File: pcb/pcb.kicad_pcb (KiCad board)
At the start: 2 copper layers, 7 parts, among them J1 Conn_01x02, J2 Conn_01x04_Male, U1 MCP73811T-420I-OT, U2 LD39050PU33R

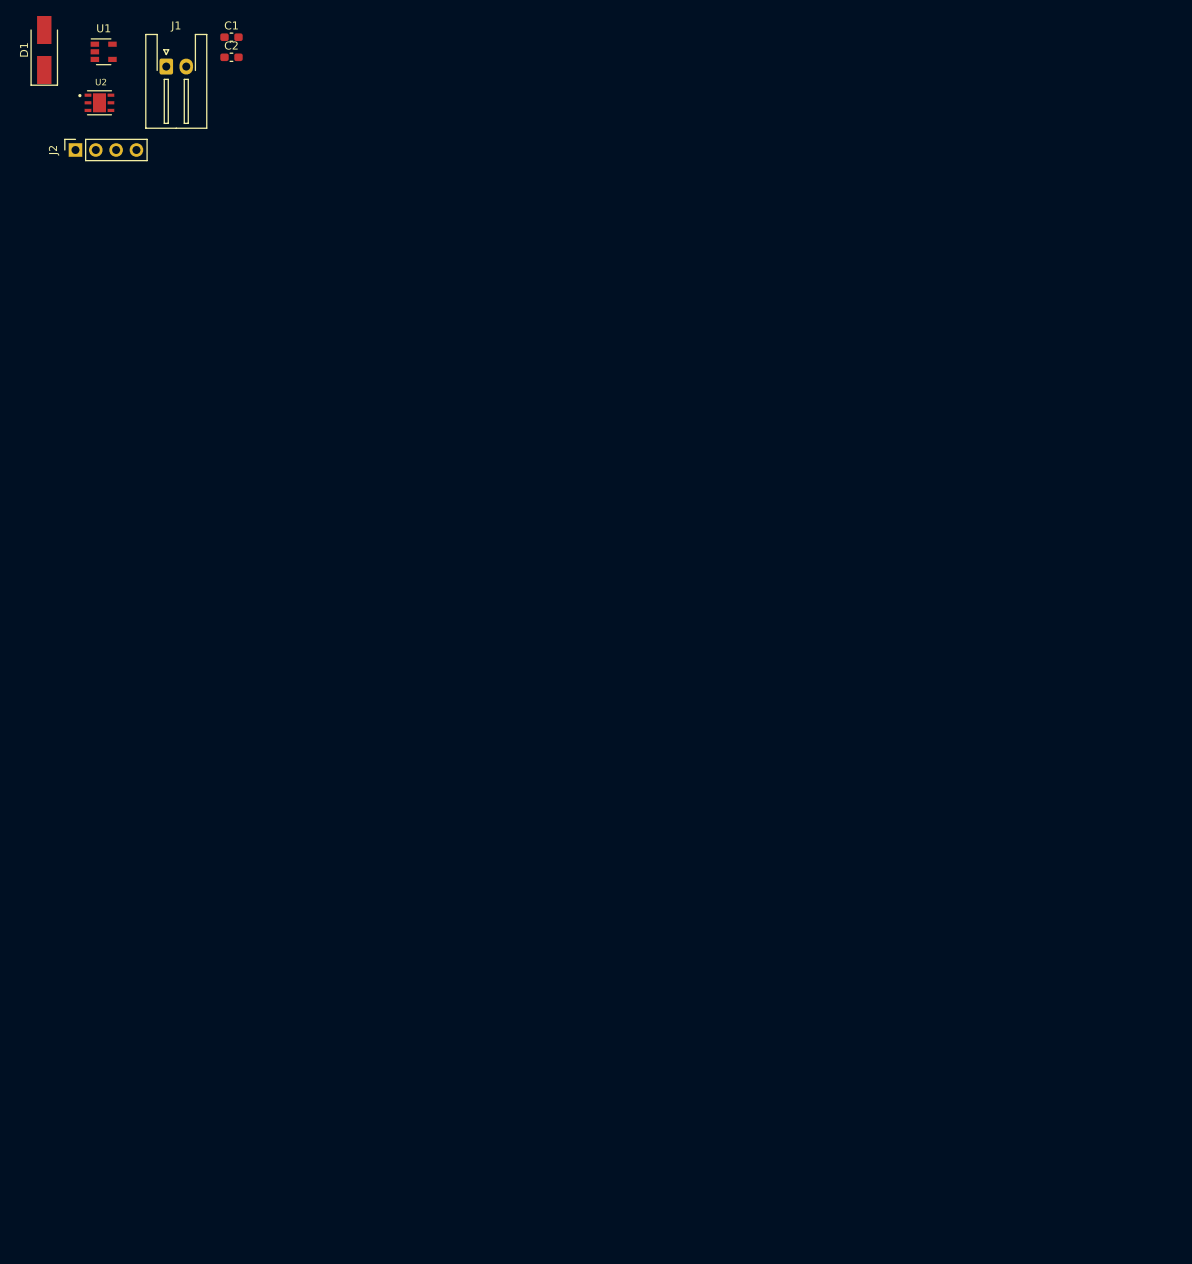
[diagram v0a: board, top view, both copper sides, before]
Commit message: finish the shcematic design
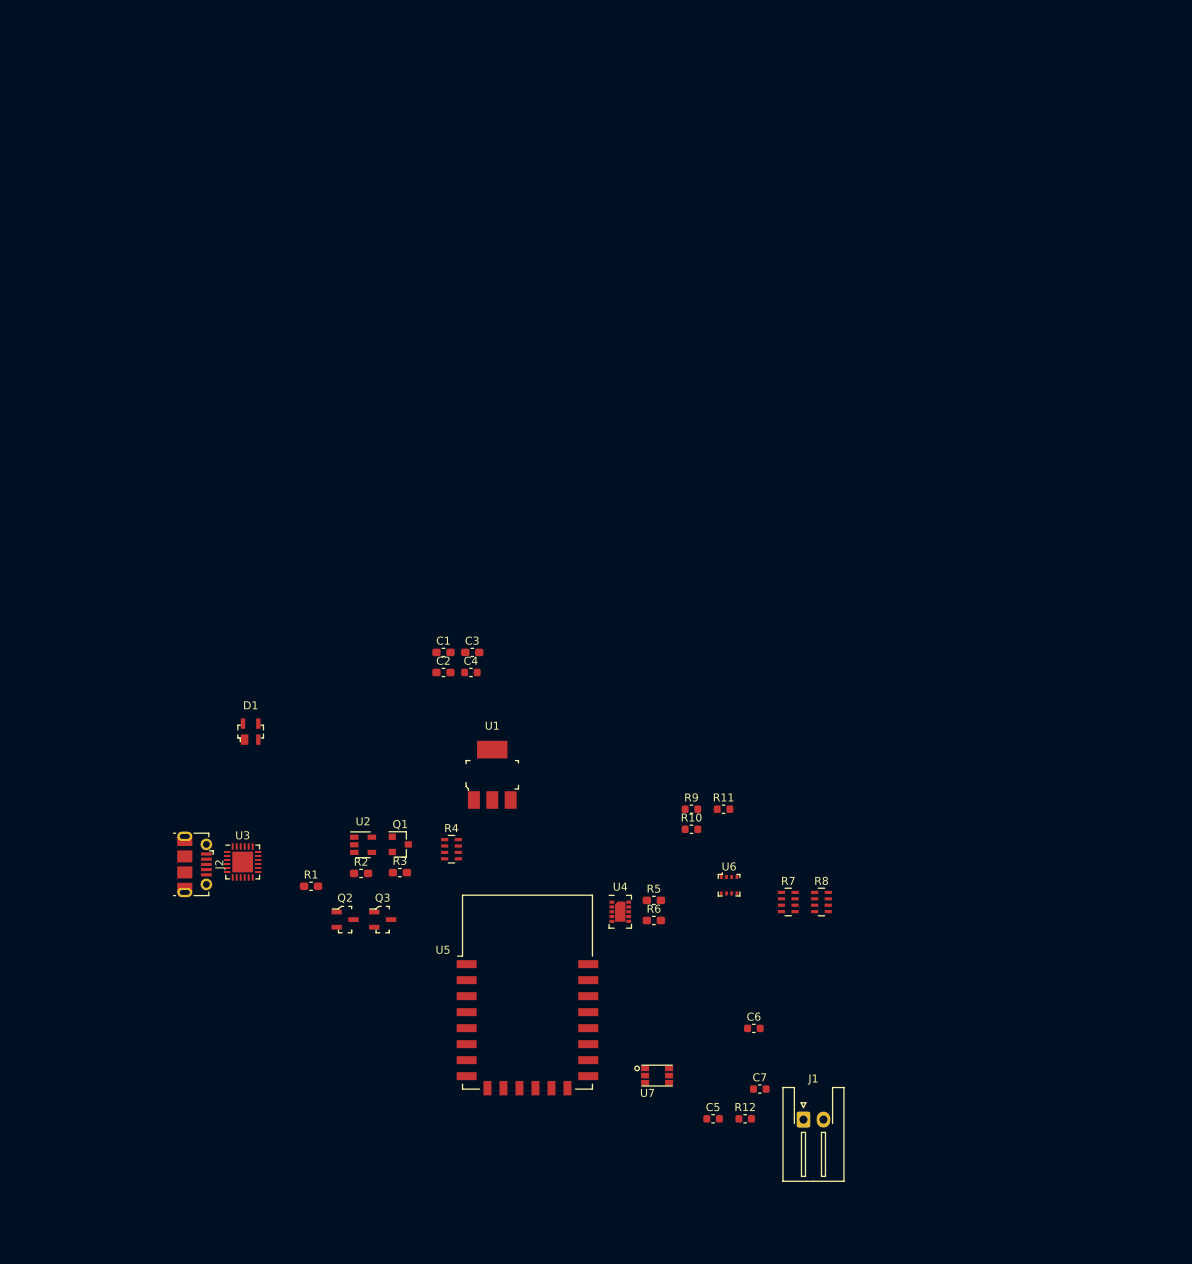
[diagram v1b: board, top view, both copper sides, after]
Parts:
- added C3: 10u, Capacitor_SMD:C_0603_1608Metric_Pad1.05x0.95mm_HandSolder, F.Cu at (53.2, 21.4)
- added C4: 100nF, Capacitor_SMD:C_0603_1608Metric, F.Cu at (53.0, 23.9)
- added C5: 100n, Capacitor_SMD:C_0603_1608Metric, F.Cu at (83.3, 79.7)
- added C6: 100n, Capacitor_SMD:C_0603_1608Metric, F.Cu at (88.4, 68.4)
- added C7: 100n, Capacitor_SMD:C_0603_1608Metric, F.Cu at (89.1, 76.0)
- added Q1: Si2371EDS, Package_TO_SOT_SMD:SOT-23, F.Cu at (44.2, 45.4)
- added Q2: MMBT2222A-TP, digikey-footprints:SOT-23-3, F.Cu at (37.3, 54.8)
- added Q3: MMBT2222A-TP, digikey-footprints:SOT-23-3, F.Cu at (42.0, 54.8)
- added R1: 2k, Resistor_SMD:R_0603_1608Metric_Pad1.05x0.95mm_HandSolder, F.Cu at (33.0, 50.6)
- added R10: 10k, Resistor_SMD:R_0603_1608Metric, F.Cu at (80.6, 43.5)
- added R11: 10k, Resistor_SMD:R_0603_1608Metric, F.Cu at (84.6, 41.0)
- added R12: 10k, Resistor_SMD:R_0603_1608Metric, F.Cu at (87.3, 79.7)
- added R2: 10k, Resistor_SMD:R_0603_1608Metric_Pad1.05x0.95mm_HandSolder, F.Cu at (39.3, 49.0)
- added R3: 10k, Resistor_SMD:R_0603_1608Metric_Pad1.05x0.95mm_HandSolder, F.Cu at (44.1, 48.9)
- added R4: R_Pack04_Split, Resistor_SMD:R_Array_Concave_4x0603, F.Cu at (50.6, 46.0)
- added R5: 100k, Resistor_SMD:R_0603_1608Metric_Pad1.05x0.95mm_HandSolder, F.Cu at (75.9, 52.4)
- added R6: 100k, Resistor_SMD:R_0603_1608Metric_Pad1.05x0.95mm_HandSolder, F.Cu at (75.9, 54.9)
- added R7: 10k, Resistor_SMD:R_Array_Concave_4x0603, F.Cu at (92.7, 52.6)
- added R8: 10k, Resistor_SMD:R_Array_Concave_4x0603, F.Cu at (96.8, 52.6)
- added R9: 10k, Resistor_SMD:R_0603_1608Metric, F.Cu at (80.6, 41.0)
- added U3: CP2104, Package_DFN_QFN:QFN-24-1EP_4x4mm_P0.5mm_EP2.6x2.6mm, F.Cu at (24.5, 47.6)
- added U4: CCS811, Package_LGA:AMS_LGA-10-1EP_2.7x4mm_P0.6mm, F.Cu at (71.7, 53.8)
- added U5: ESP-12F, RF_Module:ESP-12E, F.Cu at (60.1, 63.9)
- added U6: BME280, digikey-footprints:Pressure_Sensor_LGA-8_2.5x2.5mm_BME280, F.Cu at (85.3, 50.5)
- added U7: TSL2561, Kevin_Lutzer:TSL2561, F.Cu at (76.3, 74.3)
- C1: value 1uf -> 1u
- C2: value 1uf -> 10u
- D1: value D_Schottky -> SP0503BAHTG; footprint Diode_SMD:D_SMA_Handsoldering -> digikey-footprints:SOT-143-4
- J2: value Conn_01x04_Male -> USB_B_Micro; footprint Connector_PinSocket_2.54mm:PinSocket_1x04_P2.54mm_Vertical -> Connector_USB:USB_Micro-B_Molex-105017-0001
- U1: value MCP73811T-420I-OT -> LD1117S33CTR; footprint Package_TO_SOT_SMD:SOT-23-5 -> digikey-footprints:SOT-223
- U2: value LD39050PU33R -> MCP73831-2-OT; footprint LD39050PU33R:SON95P300X300X100-7N -> Package_TO_SOT_SMD:SOT-23-5
- moved J1 153.9 mm to (94.6, 79.8)
- moved U1 102.6 mm to (55.7, 36.7)
- moved U2 98.4 mm to (39.5, 45.5)
- moved J2 90.5 mm to (18.5, 47.9), turned to 270 degrees
- moved D1 89.0 mm to (25.5, 31.3), turned to 0 degrees
- moved C1 81.3 mm to (49.6, 21.4)
- moved C2 81.3 mm to (49.6, 23.9)
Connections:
- D1 pad 1: +5V -> GND
- D1 pad 2: +BATT -> Net-(D1-Pad2)
- J2 pad 1: (no net) -> +5V
- J2 pad 2: (no net) -> Net-(J2-Pad2)
- J2 pad 3: (no net) -> Net-(D1-Pad2)
- J2 pad 4: GND -> (no net)
- U1 pad 1: +5V -> GND
- U1 pad 2: GND -> +3V3
- U1 pad 3: +BATT -> +5V
- U1 pad 4: +5V -> +3V3
- U2 pad 1: +5V -> nBAT_STAT
- U2 pad 3: (no net) -> +BATT
- U2 pad 4: +3V3 -> +5V
- U2 pad 5: (no net) -> Net-(R1-Pad1)

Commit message: get the update done on the pcb design, finish it
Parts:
- removed R10, R11, R12: 10k, Resistor_SMD:R_0603_1608Metric
- removed R3: 10k, Resistor_SMD:R_0603_1608Metric_Pad1.05x0.95mm_HandSolder
- added D2: MBR120ESFT1G, Diode_SMD:D_SOD-123, F.Cu at (53.7, 31.6)
- added H1: MountingHole_Pad, MountingHole:MountingHole_2.2mm_M2_DIN965_Pad, F.Cu at (48.0, 74.0)
- added H2: MountingHole_Pad, MountingHole:MountingHole_2.2mm_M2_DIN965_Pad, F.Cu at (53.2, 94.0)
- added H3: MountingHole_Pad, MountingHole:MountingHole_2.2mm_M2_DIN965_Pad, F.Cu at (60.4, 86.8)
- added H4: MountingHole_Pad, MountingHole:MountingHole_2.2mm_M2, F.Cu at (48.0, 53.0)
- added SW1: PCM12, Button_Switch_SMD:SW_SPDT_PCM12, F.Cu at (125.0, 55.0)
- R2: footprint Resistor_SMD:R_0603_1608Metric_Pad1.05x0.95mm_HandSolder -> Resistor_SMD:R_Array_Convex_4x0603
- R4: value R_Pack04_Split -> 10k
- R9: footprint Resistor_SMD:R_0603_1608Metric -> Resistor_SMD:R_Array_Convex_4x1206
- U1: value LD1117S33CTR -> LD56100; footprint digikey-footprints:SOT-223 -> Package_DFN_QFN:DFN-8-1EP_2x2mm_P0.45mm_EP0.64x1.38mm
- moved R2 64.0 mm to (99.0, 72.0)
- moved J2 57.2 mm to (75.3, 54.5), turned to 180 degrees
- moved D1 54.6 mm to (72.0, 60.0)
- moved U3 54.2 mm to (77.0, 61.0), turned to 90 degrees
- moved C6 47.9 mm to (67.4, 25.4)
- moved C7 47.9 mm to (68.1, 33.0)
- moved C5 47.9 mm to (62.3, 36.7)
- moved U2 47.1 mm to (84.0, 61.0)
- moved J1 42.1 mm to (136.0, 72.0)
- moved R5 40.3 mm to (114.9, 62.4)
- moved R6 40.3 mm to (114.9, 64.9)
- moved U1 37.4 mm to (23.6, 55.9)
- moved R9 28.0 mm to (81.0, 69.0), turned to 90 degrees
- moved Q1 25.1 mm to (40.1, 20.6)
- moved Q3 25.1 mm to (37.9, 30.0)
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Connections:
- C1 pad 1: +5V -> Net-(C1-Pad1)
- Q1 pad 2: +5V -> Net-(C1-Pad1)
- R2 pad 1: +3V3 -> nBAT_STAT
- R2 pad 2: nBAT_STAT -> GND
- R9 pad 1: +3V3 -> CCS_nWAKE
- U1 pad 1: GND -> +3V3
- U1 pad 3: +5V -> Net-(R2-Pad3)
- U4 pad 1: Net-(R11-Pad2) -> Net-(R9-Pad3)
- U4 pad 2: Net-(R10-Pad2) -> Net-(R9-Pad2)
- U4 pad 7: Net-(R9-Pad2) -> CCS_nWAKE
- U5 pad 17: (no net) -> CCS_nWAKE
- U7 pad 5: Net-(R12-Pad2) -> Net-(R9-Pad4)

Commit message: try update the node modules
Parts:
- removed C1: 1u, Capacitor_SMD:C_0603_1608Metric_Pad1.05x0.95mm_HandSolder
- removed C2, C3: 10u, Capacitor_SMD:C_0603_1608Metric_Pad1.05x0.95mm_HandSolder
- removed C4: 100nF, Capacitor_SMD:C_0603_1608Metric
- removed C5, C6, C7: 100n, Capacitor_SMD:C_0603_1608Metric
- removed D1: SP0503BAHTG, digikey-footprints:SOT-143-4
- removed D2: MBR120ESFT1G, Diode_SMD:D_SOD-123
- removed J2: USB_B_Micro, Connector_USB:USB_Micro-B_Molex-105017-0001
- removed Q1: Si2371EDS, Package_TO_SOT_SMD:SOT-23
- removed Q2, Q3: MMBT2222A-TP, digikey-footprints:SOT-23-3
- removed R1: 2k, Resistor_SMD:R_0603_1608Metric_Pad1.05x0.95mm_HandSolder
- removed R2: 10k, Resistor_SMD:R_Array_Convex_4x0603
- removed R4, R7, R8: 10k, Resistor_SMD:R_Array_Concave_4x0603
- removed R5, R6: 100k, Resistor_SMD:R_0603_1608Metric_Pad1.05x0.95mm_HandSolder
- removed R9: 10k, Resistor_SMD:R_Array_Convex_4x1206
- removed U1: LD56100, Package_DFN_QFN:DFN-8-1EP_2x2mm_P0.45mm_EP0.64x1.38mm
- removed U2: MCP73831-2-OT, Package_TO_SOT_SMD:SOT-23-5
- removed U3: CP2104, Package_DFN_QFN:QFN-24-1EP_4x4mm_P0.5mm_EP2.6x2.6mm
- removed U4: CCS811, Package_LGA:AMS_LGA-10-1EP_2.7x4mm_P0.6mm
- removed U6: BME280, digikey-footprints:Pressure_Sensor_LGA-8_2.5x2.5mm_BME280
- removed U7: TSL2561, Kevin_Lutzer:TSL2561
- added SW2: PTS645Vx83, Button_Switch_THT:SW_Tactile_SPST_Angled_PTS645Vx58-2LFS, F.Cu at (86.5, 58.2)
- added SW3: PTS645Vx83, Button_Switch_THT:SW_Tactile_SPST_Angled_PTS645Vx58-2LFS, F.Cu at (75.8, 58.2)
- H1: footprint MountingHole:MountingHole_2.2mm_M2_DIN965_Pad -> MountingHole:MountingHole_2.2mm_M2
- H2, H3: footprint MountingHole:MountingHole_2.2mm_M2_DIN965_Pad -> MountingHole:MountingHole_2.2mm_M2_ISO14580_Pad
- J1: value Conn_01x02 -> USB_B_Mini; footprint Connector_JST:JST_XH_S2B-XH-A-1_1x02_P2.50mm_Horizontal -> Connector_USB:USB_Micro-B_Molex-105017-0001
- SW1: value PCM12 -> OS102011MA1QN1‎; footprint Button_Switch_SMD:SW_SPDT_PCM12 -> Button_Switch_THT:SW_CuK_OS102011MA1QN1_SPDT_Angled
- moved H2 56.7 mm to (97.0, 58.0)
- moved SW1 47.4 mm to (86.0, 82.0)
- moved J1 38.7 mm to (97.3, 70.0), turned to 90 degrees
- moved H3 36.9 mm to (97.0, 82.0)
- moved H4 29.4 mm to (43.0, 82.0)
- moved H1 16.8 mm to (43.0, 58.0)
- moved U5 10.4 mm to (52.2, 70.0), turned to 90 degrees
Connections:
- H1 pad 1: GND -> (no net)
- H4 pad 1: GND -> (no net)
- J1 pad 1: GND -> +5V
- J1 pad 2: +BATT -> Net-(J1-Pad2)
- SW1 pad 1: +3V3 -> GND
- SW1 pad 3: GND -> +3V3
- U5 pad 17: CCS_nWAKE -> RGB_LED
- U5 pad 2: BAT_LVL -> (no net)
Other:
- board outline added: 60 x 30 mm

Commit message: update the pcb stuff
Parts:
- added C1: 100n, Capacitor_SMD:C_0603_1608Metric, F.Cu at (69.5, 42.5)
- added C10: 1u, Capacitor_SMD:C_0603_1608Metric, F.Cu at (69.5, 45.0)
- added C2: 47u, Capacitor_SMD:C_0805_2012Metric, F.Cu at (58.6, 47.2)
- added C3: 100n, Capacitor_SMD:C_0603_1608Metric, F.Cu at (73.5, 45.0)
- added C4: 100n, Capacitor_SMD:C_0603_1608Metric, F.Cu at (131.0, 37.0)
- added C5: 100n, Capacitor_SMD:C_0603_1608Metric, F.Cu at (77.7, 39.1)
- added C6: 100n, Capacitor_SMD:C_0603_1608Metric, F.Cu at (73.7, 39.1)
- added C8: 10u, Capacitor_SMD:C_0805_2012Metric, F.Cu at (73.5, 42.5)
- added C9: 100n, Capacitor_SMD:C_0603_1608Metric, F.Cu at (80.1, 36.6)
- added D1: WS2812B, LED_SMD:LED_WS2812B_PLCC4_5.0x5.0mm_P3.2mm, F.Cu at (60.6, 36.2)
- added D2: SP0503BAHT, Package_TO_SOT_SMD:SOT-143, F.Cu at (67.4, 35.1)
- added J2: Conn_01x04_Male, Connector_PinHeader_2.54mm:PinHeader_1x04_P2.54mm_Vertical, F.Cu at (94.9, 33.4)
- added R2: 10k, Resistor_SMD:R_0603_1608Metric, F.Cu at (76.1, 36.6)
- added R3: 10k, Resistor_SMD:R_0603_1608Metric, F.Cu at (80.1, 34.1)
- added R4: 10k, Resistor_SMD:R_0603_1608Metric, F.Cu at (76.1, 34.1)
- added R5: 10k, Resistor_SMD:R_Array_Convex_4x0603, F.Cu at (64.7, 46.5)
- added RN1: 10k, Resistor_SMD:R_Array_Convex_4x0603, F.Cu at (99.3, 33.5)
- added SW1: PTS645Vx83, Button_Switch_THT:SW_Tactile_SPST_Angled_PTS645Vx58-2LFS, F.Cu at (121.4, 37.5)
- added U1: AP2112K-3.3, Package_TO_SOT_SMD:SOT-23-5, F.Cu at (131.4, 33.4)
- added U2: MIC5225-1.8YM5, Package_TO_SOT_SMD:SOT-23-5, F.Cu at (65.1, 41.8)
- added U3: CP2104, Package_DFN_QFN:QFN-24-1EP_4x4mm_P0.5mm_EP2.6x2.6mm, F.Cu at (59.5, 42.6)
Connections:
- SW1 pad 2: Net-(R2-Pad1) -> (no net)
- U5 pad 14: (no net) -> MODE
